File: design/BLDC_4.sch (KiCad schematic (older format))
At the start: 25 parts, among them K1 SERVO, P1 HALL/Encoder, P3 PWR_COMM, P4 IN+, P5 IN-, P6 MOTOR1, P7 MOTOR2, P9 MOTOR3, X1 MINI-USB-SHIELD-32005-201

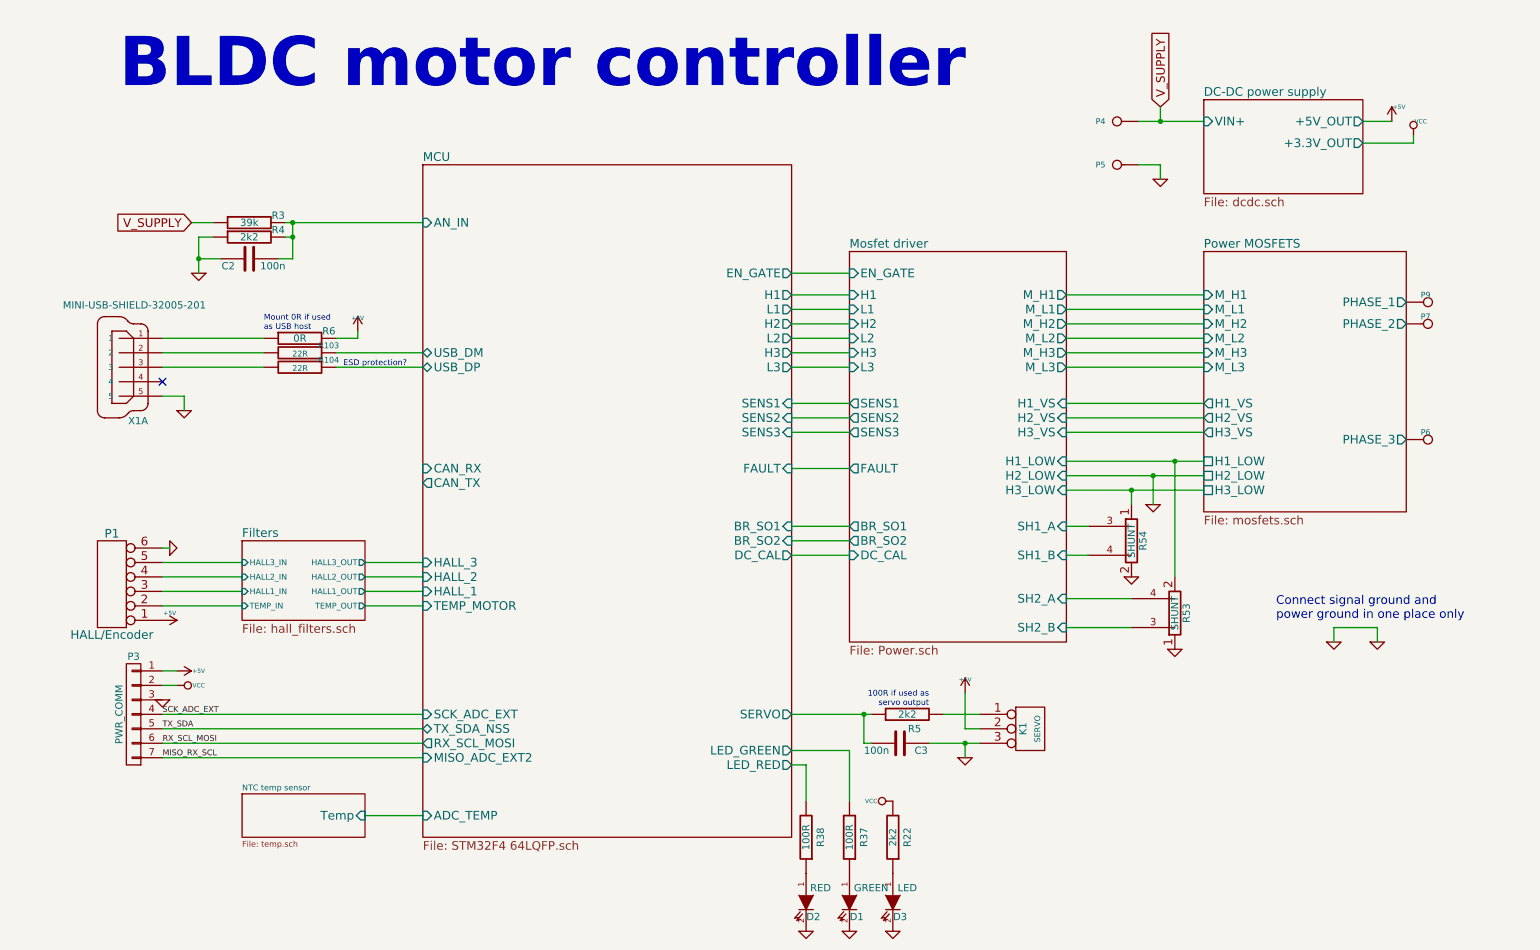
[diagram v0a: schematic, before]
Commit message: schema mods done
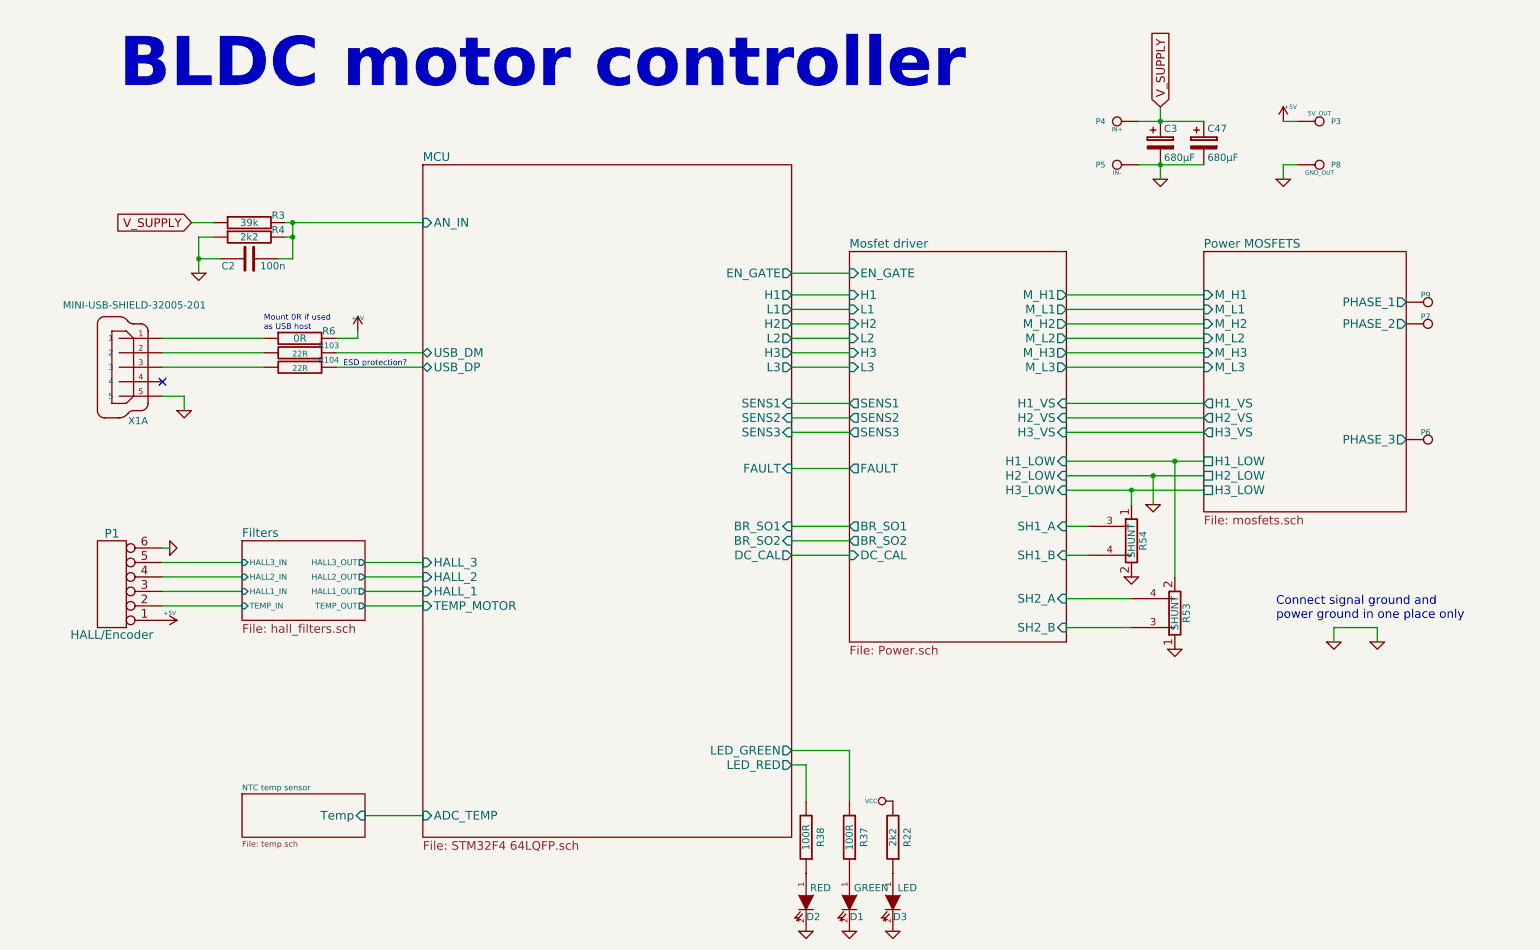
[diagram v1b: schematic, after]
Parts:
- removed C3: 100n, CRF1:SMD-0603_c, symbol C-RESCUE-BLDC_4
- removed K1: SERVO, CRF1:pinhead-1X03, symbol CONN_3
- removed P3: PWR_COMM, CRF1:b7b-ph-kl, symbol CONN_01X07
- removed R5: 2k2, CRF1:SMD-0603_r, symbol R-RESCUE-BLDC_4
- added C3, C47: 680µF, symbol CP
- added P3: 5V_OUT, CRF1:1PAD_4x5mm, symbol CONN_1
- added P8: GND_OUT, CRF1:1PAD_4x5mm, symbol CONN_1
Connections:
- net +5V: now also P3.1
- net GND: now also C3.2, C47.2, P8.1
- net V_SUPPLY: now also C3.1, C47.1
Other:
- note removed: "100R if used as\nservo output"
